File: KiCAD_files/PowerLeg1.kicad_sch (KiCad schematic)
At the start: 71 parts, among them J201 Conn_01x01, J202 Conn_01x01, J203 Conn_01x01, J204 Conn_01x01, J205 Conn_01x01, J206 Conn_01x01, J207 Conn_01x01, J208 Conn_01x01, J209 Conn_01x01, J210 Conn_01x01, Q201 IPD200N15N3, Q202 IPD200N15N3, Q203 IPD200N15N3, U201 AMC1100DUB, U202 ACS730xLCTR-20AB, U203 UCC21222DR, U204 OPA316, U205 OPA316, U206 SFH617A-2X009T

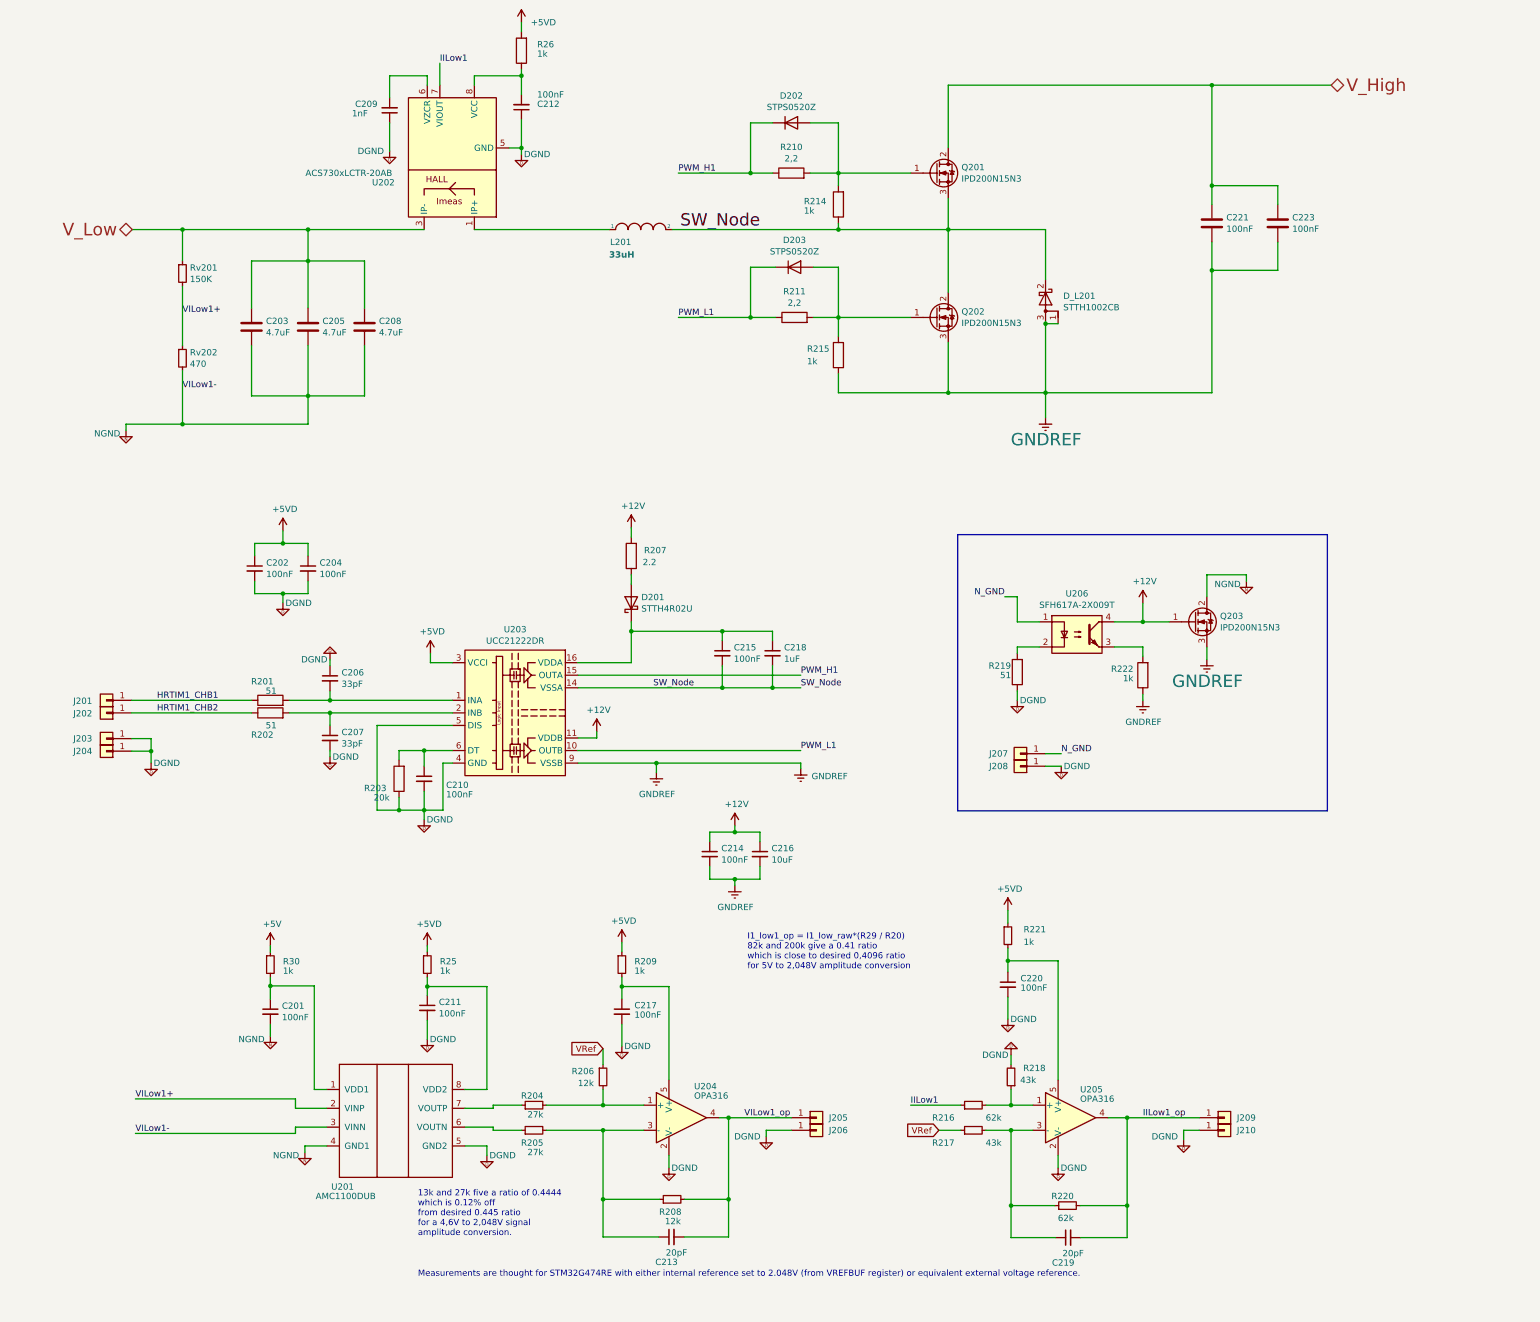
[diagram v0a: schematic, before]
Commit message: Edited opamp comments that were outdated.
Former-commit-id: 22e139dd8e717e45edbeb5b70fb47a644a62ae14
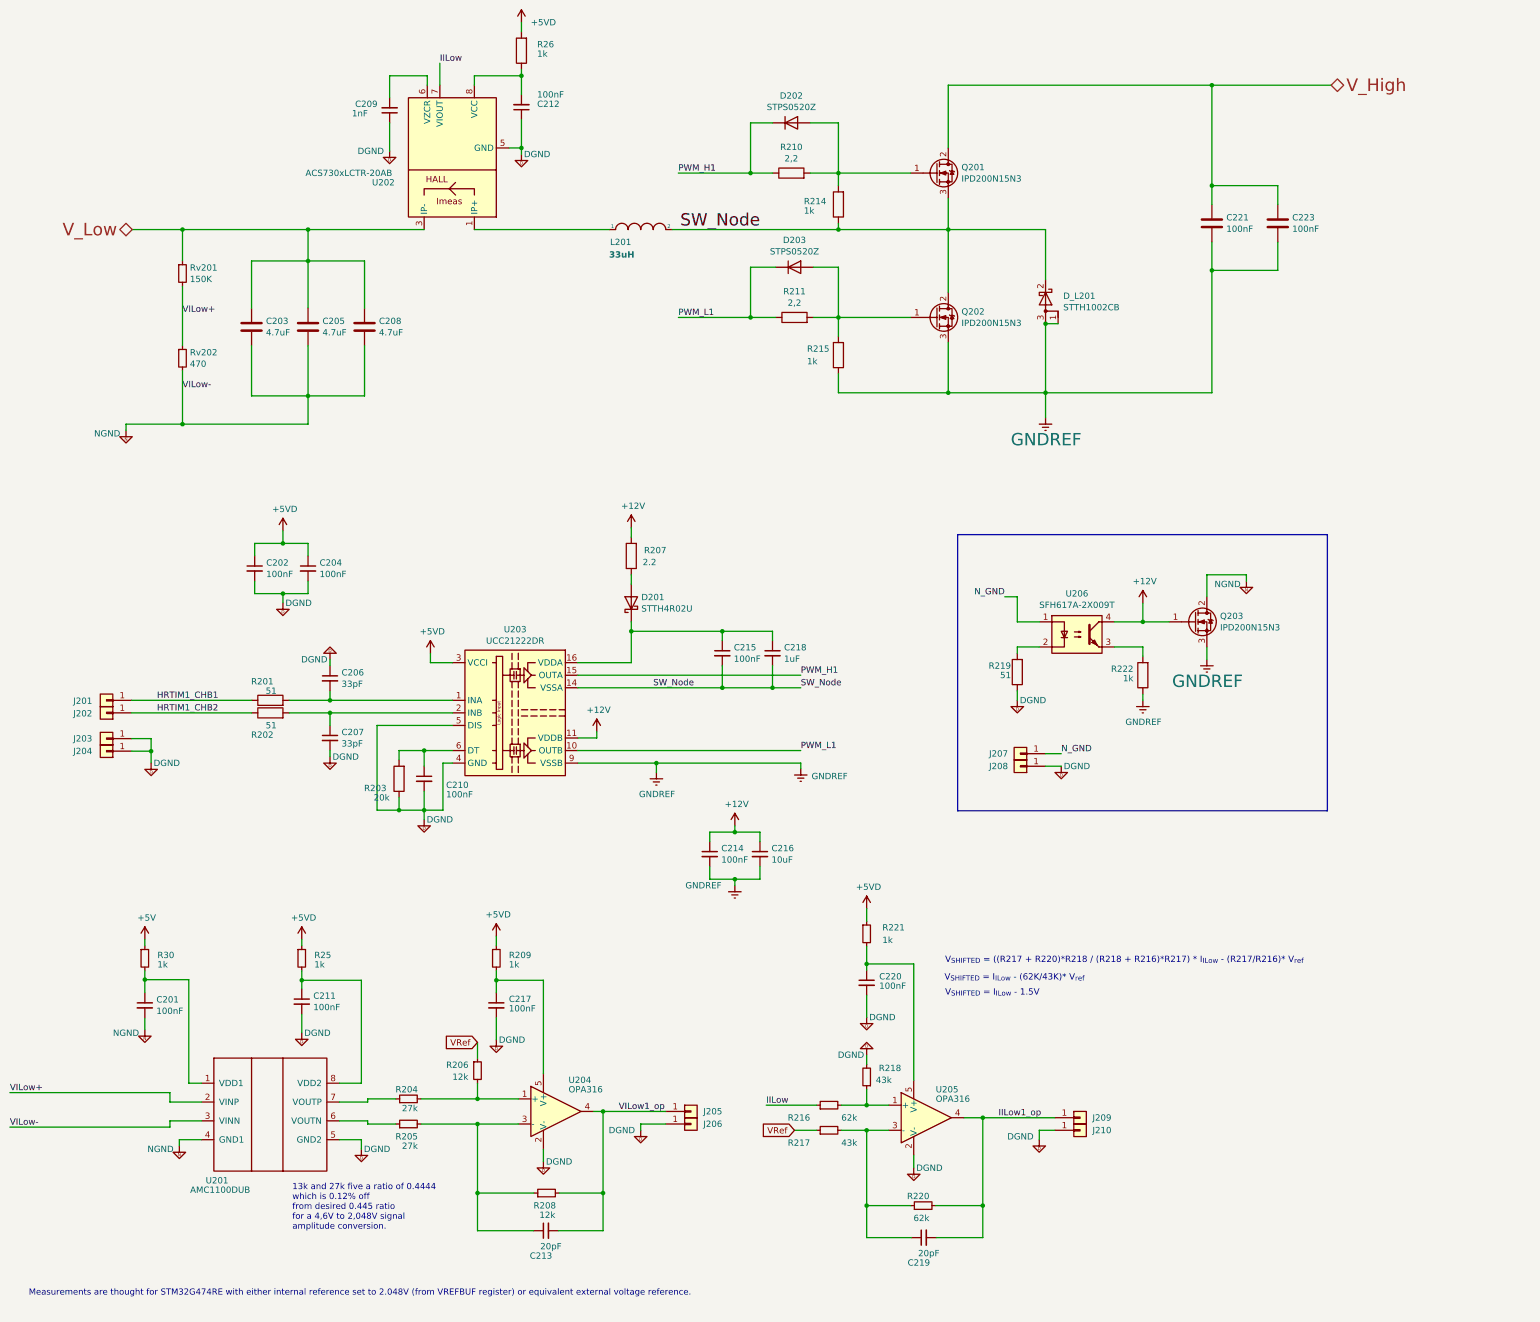
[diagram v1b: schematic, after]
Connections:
- net IILow1 renamed IILow
- net VILow1+ renamed VILow+
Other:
- note added: "V_{SHIFTED} = ((R217 + R220)*R218 / (R218 + R216)*R217) * I_{ILow} - (R217/R216)* V_{ref}"
- note added: "V_{SHIFTED} = I_{ILow} - (62K/43K)* V_{ref}"
- note added: "V_{SHIFTED} = I_{ILow} - 1.5V"
- note removed: "I1_low1_op = I1_low_raw*(R29 / R20) 82k and 200k give a 0.41 ratio which is close to desired 0,4096 ratio for 5V to 2,048V amplitude conversion"
- moved on the sheet: C201, C211, C213, C217, C219, C220, J205, J206, J209, J210, R204, R205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

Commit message: [Power] Finished routing all the tracks, no more rastnet, ready for refining
Former-commit-id: c85419efed005dbd6b325ef0aef7156952f8cebe
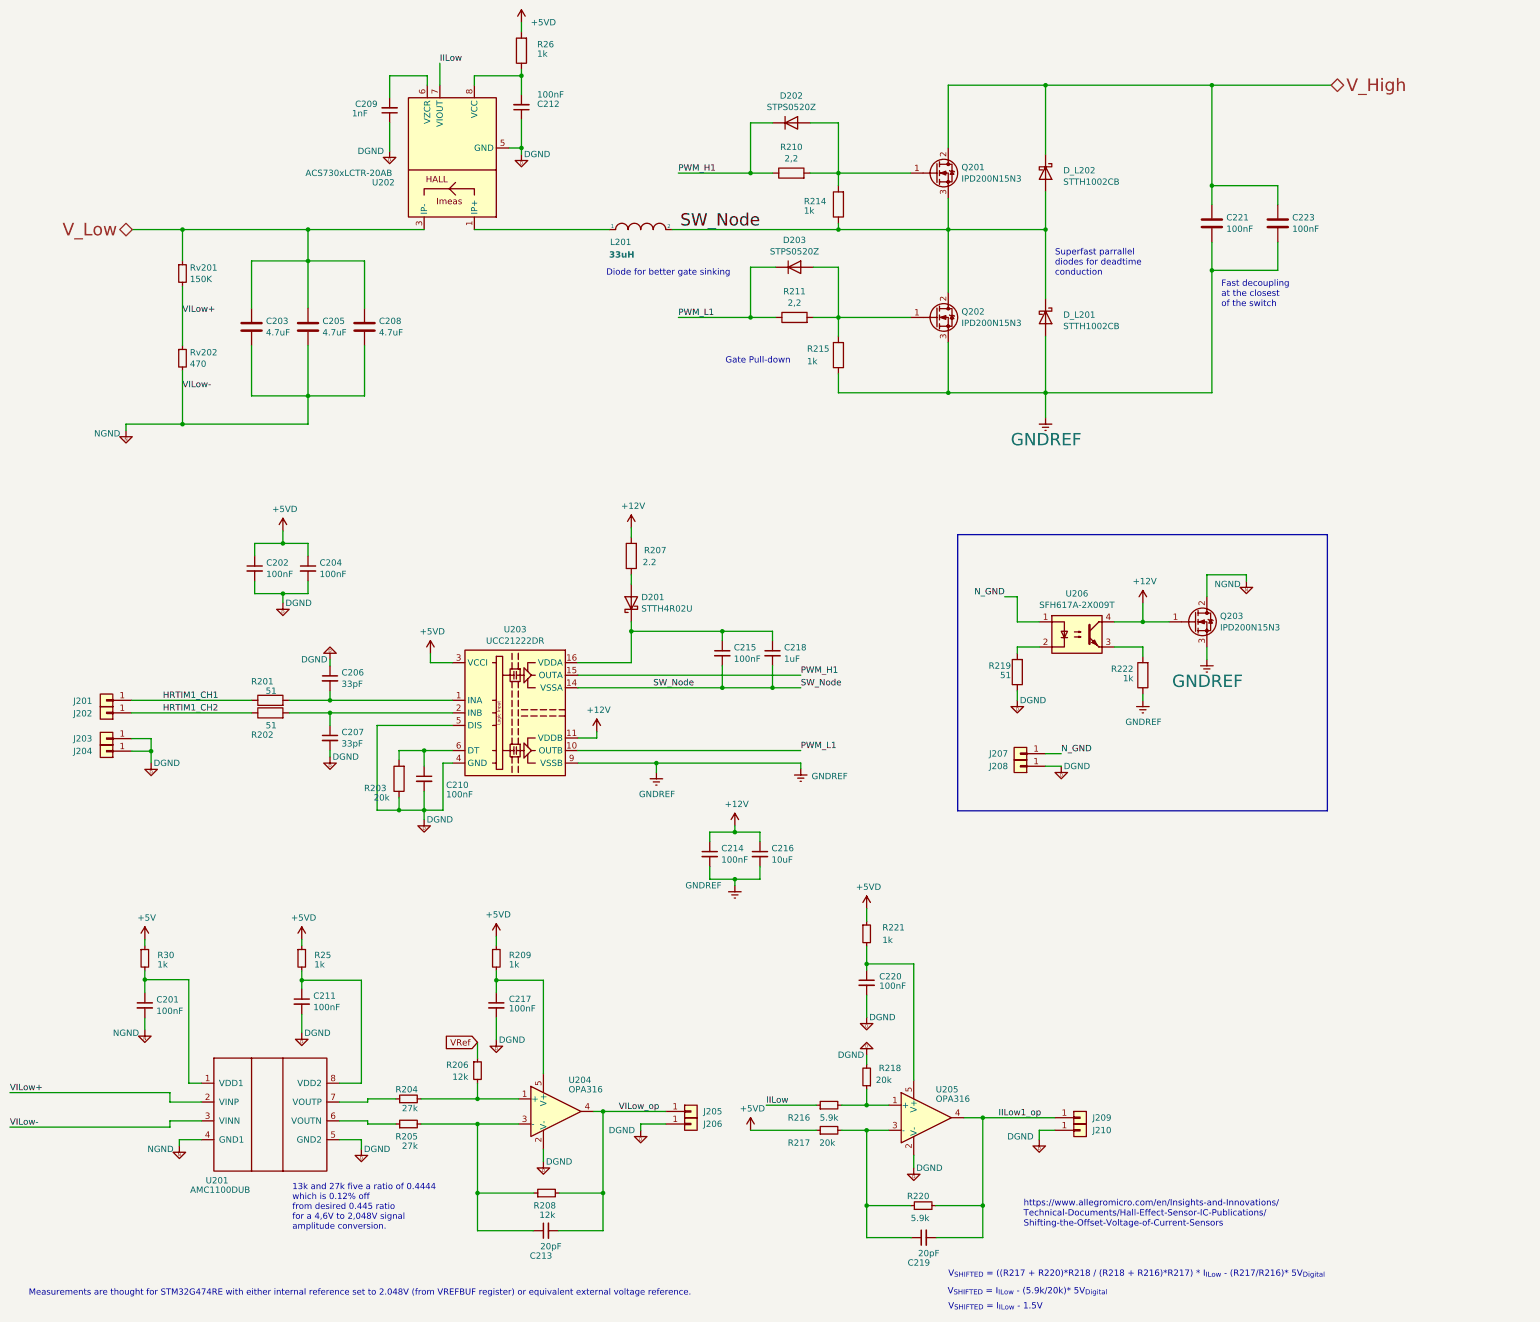
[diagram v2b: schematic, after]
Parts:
- added D_L202: STTH1002CB, Diode_SMD:D_SOD-123, symbol Device:D_Schottky
- C201, C211, C212: footprint Capacitor_SMD:C_0805_2012Metric -> Capacitor_SMD:C_1206_3216Metric
- D_L201: symbol Device:D_Schottky_AKA -> Device:D_Schottky
- R216, R220: value 62k -> 5.9k
- R217, R218: value 43k -> 20k
- U201: footprint Package_SO:SOP-8_6.62x9.15mm_P2.54mm -> Footprints:SOP-8_6.62x9.15mm_P2.54mm
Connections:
- net +5VD: now also R217.1
- net GNDREF: now also D_L201.2 (A); no longer D_L201.1 (A), D_L201.3 (A)
- net SW_Node: now also D_L201.1 (K), D_L202.2 (A); no longer D_L201.2 (K)
- net VRef: no longer R217.1
- net V_High: now also D_L202.1 (K)
- net HRTIM1_CHB1 renamed HRTIM1_CH1
- net HRTIM1_CHB2 renamed HRTIM1_CH2
- net VILow1_op renamed VILow_op
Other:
- note added: "Diode for better gate sinking"
- note added: "Fast decoupling at the closest of the switch"
- note added: "Gate Pull-down"
- note added: "Superfast parrallel diodes for deadtime conduction"
- note added: "V_{SHIFTED} = ((R217 + R220)*R218 / (R218 + R216)*R217) * I_{ILow} - (R217/R216)* 5V_{Digital}"
- note added: "V_{SHIFTED} = I_{ILow} - (5.9k/20k)* 5V_{Digital}"
- note added: "https://www.allegromicro.com/en/Insights-and-Innovations/ Technical-Documents/Hall-Effect-Sensor-IC-Publications/ Shifting-the-Offset-Voltage-of-Current-Sensors"
- note removed: "V_{SHIFTED} = ((R217 + R220)*R218 / (R218 + R216)*R217) * I_{ILow} - (R217/R216)* V_{ref}"
- note removed: "V_{SHIFTED} = I_{ILow} - (62K/43K)* V_{ref}"

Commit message: Supressed backup files
Former-commit-id: af6064aba0445a9773bde6e74b771947025d2895
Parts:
- renumbered C201 to C1, C210 to C10, C211 to C11, C212 to C12, C213 to C13, C214 to C14, C215 to C15, C216 to C16, C217 to C17, C218 to C18, C219 to C19, C202 to C2, C220 to C20, C221 to C21, C223 to C23, C203 to C3, C204 to C4, C205 to C5, C206 to C6, C207 to C7, C208 to C8, C209 to C9, D201 to D1, D202 to D2, D203 to D3, D_L201 to D_L1, D_L202 to D_L3, J201 to J1, J210 to J10, J202 to J2, J203 to J3, J204 to J4, J205 to J5, J206 to J6, J207 to J7, J208 to J8, J209 to J9, L201 to L1, Q201 to Q1, Q202 to Q2, Q203 to Q3, R201 to R1, R210 to R10, R211 to R11, R214 to R14, R215 to R15, R216 to R16, R217 to R17, R218 to R18, R219 to R19, R202 to R2, R220 to R20, R221 to R21, R222 to R22, R25 to R27, R26 to R28, R203 to R3, R30 to R31, R204 to R4, R205 to R5, R206 to R6, R207 to R7, R208 to R8, R209 to R9, Rv201 to Rv1, Rv202 to Rv2, U201 to U1, U202 to U2, U203 to U3, U204 to U4, U205 to U5, U206 to U6
